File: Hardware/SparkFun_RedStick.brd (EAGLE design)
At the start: 17.8 x 66 mm, 42 parts, among them Q1 DMG2307L, Q2 MOSFET-NCHANNEL2N7002PW, U1 FTS31XS-U, U2 ATMEGA328P_TQFP, U4 5.0v, Y1 16MHZ

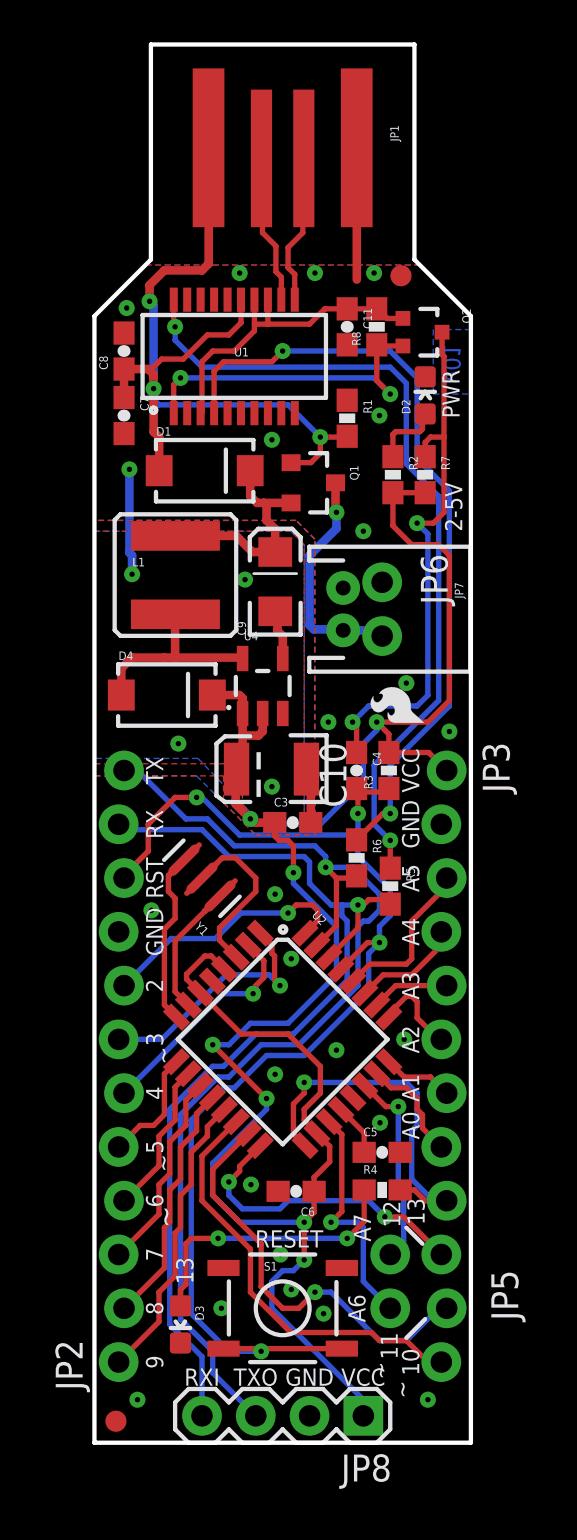
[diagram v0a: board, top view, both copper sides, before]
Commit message: Hardware changes for reds review
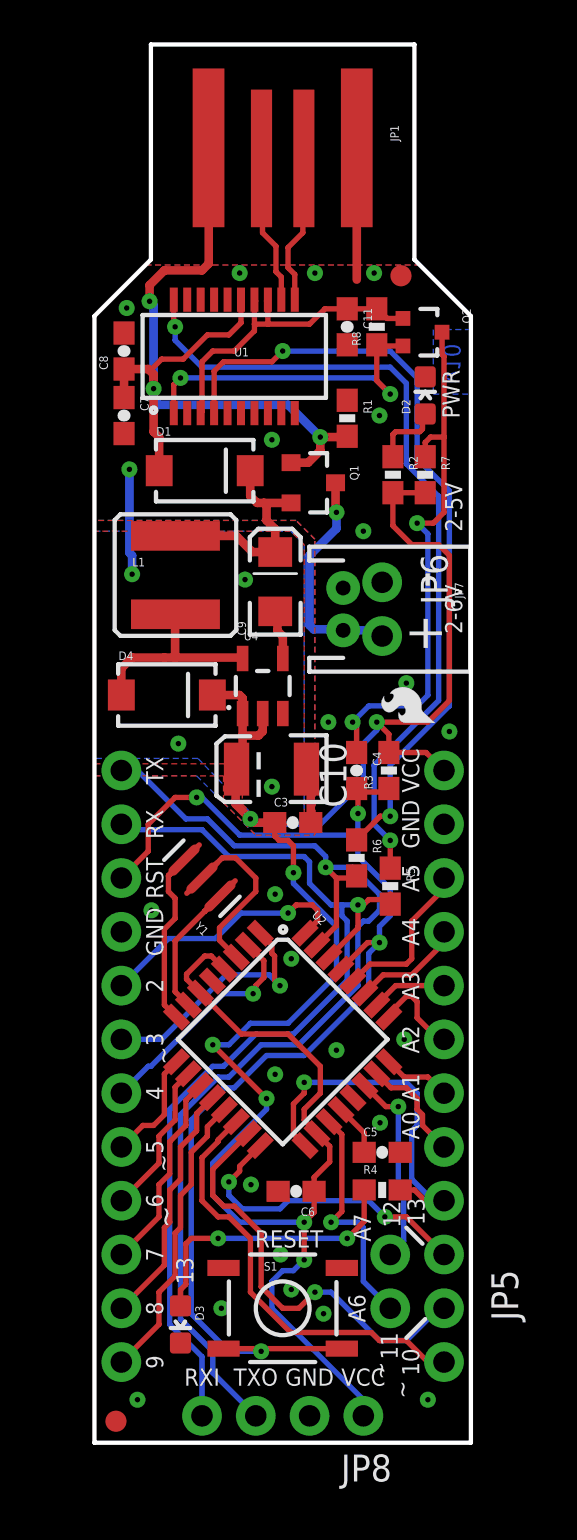
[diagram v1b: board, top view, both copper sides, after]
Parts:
- JP2, JP3: device SparkFun-Connectors:1X12_LOCK_NO_SILK -> SparkFun-Connectors:1X12_NO_SILK
- JP8: device SparkFun-Connectors:1X04 -> SparkFun-Connectors:1X04_NO_SILK_ALL_ROUND
- R2: value 10K -> 6.8K
- R4: value 330 -> 2.2k
- moved LOGO1 0.51 mm to (16.4, 33.7)
- moved U$1 0.36 mm to (10.7, 43.7)
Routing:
- net D10: track 20.1 -> 20.6 mm
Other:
- board text added: "2-6V"
- board text added: "v10"
- board text removed: "0"
- board text removed: "1"
- board text removed: "v01"
